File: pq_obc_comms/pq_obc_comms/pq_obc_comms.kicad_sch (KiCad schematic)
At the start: 66 parts, among them J1 Conn_01x10, J2 Conn_01x10, J3 Conn_01x10, J4 Conn_01x10, J6 U.FL-R-SMT-1_10_, U1 STM32L476RGTx, U2 SX1262IMLTRT, U3 BD2232G-GTR, U4 BD2232G-GTR, U5 RFswitch, U7 BD2232G-GTR, X1 12MHz, X2 FA-128_32.0000MF20X-K5, X3 32.768KHz

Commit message: Cleanup!
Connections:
- net 3V3: no longer J1.10 (Pin_10)
- new net 3V3_PERM: J1.10 (Pin_10)
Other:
- moved on the sheet: C45, J3, U3

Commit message: obc rework
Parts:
- removed C40, C41: 20pF, symbol COMMS-altium-import:3_20pF
- removed D2: VCC_TEST, symbol COMMS-altium-import:0_VCC_TEST
- removed J6: U.FL-R-SMT-1_10_, symbol COMMS-altium-import:1_U.FL-R-SMT-1_10_
- removed PROBE1: MS-156C, GGS_Connectors:CoaxialSwitch_Hirose_MS-156C3_Horizontal, symbol GGS_Connectors:MS-156C
- removed X1: 12MHz, GGS_Miscellaneous:ECX-32, symbol COMMS-altium-import:0_12MHz
- added C40: 20pF, Capacitor_SMD:C_0603_1608Metric, symbol COMMS-altium-import:3_10pF
- added C41: 20pF, Capacitor_SMD:C_0603_1608Metric, symbol COMMS-altium-import:3_100nF
- added D2: RBS1LAM40ATR, Diode_SMD:D_SOD-128, symbol Simulation_SPICE:DIODE
- added J6: U.FL-R-SMT-1_10, Connector_Coaxial:U.FL_Hirose_U.FL-R-SMT-1_Vertical, symbol Connector:Conn_Coaxial
- added TP1: CoaxialSwitch_Testpoint, symbol Connector:CoaxialSwitch_Testpoint
- added X1: ECS-120-18-33-JEM-TR3, GGS_Miscellaneous:ECX-32, symbol Device:Crystal_GND24
- C1, C11, C12, C2, C4, C5, C6, C7, C8: footprint (none) -> Capacitor_SMD:C_0402_1005Metric
- C10, C9: footprint (none) -> Capacitor_SMD:C_0402_1005Metric; symbol COMMS-altium-import:3_3.3pF -> Device:C
- C14, C15, C16, C17, C18, C27, C28, C42, C43, C44, C45: footprint (none) -> Capacitor_SMD:C_0603_1608Metric
- D1: value VCC -> RBS1LAM40ATR; footprint (none) -> Diode_SMD:D_SOD-128; BOM_JLCPCB PART CLASS Extended Part -> (none); BOM_MANUFACTURER ROHM Semicon -> (none); BOM_MANUFACTURER PART PDZVTR4.7B -> (none); BOM_SUPPLIER LCSC -> (none); BOM_SUPPLIER PART C253498 -> (none)
- L1, L2, L3, L4, L5, L6: footprint (none) -> Inductor_SMD:L_0402_1005Metric
- L7: footprint (none) -> Inductor_SMD:L_0805_2012Metric
- R3, R4, R6, R7, R8: footprint (none) -> Resistor_SMD:R_0603_1608Metric
- U2: footprint (none) -> Package_DFN_QFN:QFN-24-1EP_4x4mm_P0.5mm_EP2.6x2.6mm
- U3, U4, U7: footprint (none) -> Package_TO_SOT_SMD:SOT-23-5
- U5: value RFswitch -> BGS12PL6E6327XTSA1; footprint (none) -> GGS_RF:PG-TSLP-6-4; BOM_SUPPLIER PART C1854968 -> BGS12PL6E6327XTSA1
- X3: value 32.768KHz -> ABS09-32.768KHZ-7-T; footprint (none) -> GGS_Miscellaneous:ABS09; BOM_SUPPLIER LCSC -> (none); BOM_SUPPLIER PART C1985392 -> (none)
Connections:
- net ADC_PH: now also J4.5 (Pin_5); no longer J4.6 (Pin_6)
- net ADC_PL: now also J2.9 (Pin_9); no longer J2.2 (Pin_2)
- net CHRG: now also J4.10 (Pin_10); no longer J4.1 (Pin_1)
- net CHRGOFF: now also J2.4 (Pin_4); no longer J2.7 (Pin_7)
- net CLPROG: now also J2.3 (Pin_3); no longer J2.8 (Pin_8)
- net DAC_PL: now also J2.8 (Pin_8); no longer J2.3 (Pin_3)
- net EPS_RST: no longer J3.10 (Pin_10)
- net FAULT: now also J4.9 (Pin_9); no longer J4.2 (Pin_2)
- net GND: now also C40.2, C41.2, J6.2 (Ext), TP1.G, X1.2, X1.4
- net MPPT_X: no longer J2.9 (Pin_9)
- net MPPT_Y: no longer J4.8 (Pin_8)
- net MPPT_Z: no longer J4.9 (Pin_9)
- net NRST: now also J2.5 (Pin_5); no longer J2.6 (Pin_6)
- net OSC_IN: now also C40.1, X1.1
- net OSC_OUT: now also C41.1, X1.3
- net P/L_POWER: now also J4.6 (Pin_6); no longer J4.5 (Pin_5)
- net RST_DRIVERS: now also J4.4 (Pin_4); no longer J4.7 (Pin_7)
- net SEL_PH0: now also J4.7 (Pin_7); no longer J4.4 (Pin_4)
- net SOLAR_X: now also J2.1 (Pin_1); no longer J2.10 (Pin_10)
- net SOLAR_Z: now also J4.1 (Pin_1); no longer J4.10 (Pin_10)
- net STM32_PA2: now also J2.10 (Pin_10); no longer J2.1 (Pin_1)
- net STM32_PD2: now also J4.2 (Pin_2); no longer J3.3 (Pin_3)
- net SWCLK: now also J2.7 (Pin_7); no longer J2.4 (Pin_4)
- net SWDIO: now also J2.6 (Pin_6); no longer J2.5 (Pin_5)
- net VCC: now also D2.2 (K); no longer J4.3 (Pin_3)
- net at L2.2: now also TP1.C
- net at C10.1, L5.2: now also J6.1 (In)
- net at C4.1, L1.2, L3.1: now also TP1.A
- net P/L2BURN renamed ADCS_POWER
- net ADCS_POWER: now also J4.3 (Pin_3)
- new net BATT_NTC: J3.3 (Pin_3)
- new net VCC_UMBILICAL: D2.1 (A), J4.8 (Pin_8)
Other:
- note removed: "To be done in PL2 board"
- note removed: "Vcc Test"
- moved on the sheet: C1, C14, C2, C27, C28, C31, C32, C33, C34, C35, C36, C37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

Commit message: OBC board revision 3 finished
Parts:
- added C3: 100nF, Capacitor_SMD:C_0603_1608Metric, symbol Device:C
- TP1: footprint (none) -> Connector_Coaxial:CoaxialSwitch_Hirose_MS-156C3_Horizontal
- X2: footprint (none) -> GGS_Miscellaneous:EPSON_FA128
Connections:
- net 3V3 is gone; now on net 3V3_PERM: D1.1 (A)
- net BUSY is gone; now on net SX1262_BUSY: U1.41 (PA8)
- net CHGOFF is gone; now on net CHRGOFF: U1.8 (PC0)
- net P/L2BURN_OBC is gone; now on net PoL_ADCS_POWER_EN: U4.3 (EN/EN#)
- net SEL_PH3 is gone; now on net SEL_PH0: U1.10 (PC2)
- net GND: now also J3.10 (Pin_10), C3.2
- net PoL_P/L_EN: now also U1.37 (PC6); no longer U1.11 (PC3)
- net VCC: now also C3.1
- net RFswitch_Vcc: now reaches C14.1, R4.2, U5.4 (VDD)
- net DIO2: now reaches R3.1, U2.12 (DIO2)
- net EPS_RST renamed STM32_PB0
- net STM32_PB0: now also J4.2 (Pin_2)
- net MPPT_X: no longer names the net of U1.22 (PA6)
- net MPPT_Y: no longer names the net of U1.27 (PB1)
- net MPPT_Z renamed PoL_ADCS_POWER_EN
- net STM32_PD2: no longer names the net of U1.54 (PD2)
- net STM32_PD2: no longer J4.2 (Pin_2)
- no-connect marks 14 -> 13
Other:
- moved on the sheet: C14, C16, C18, R4

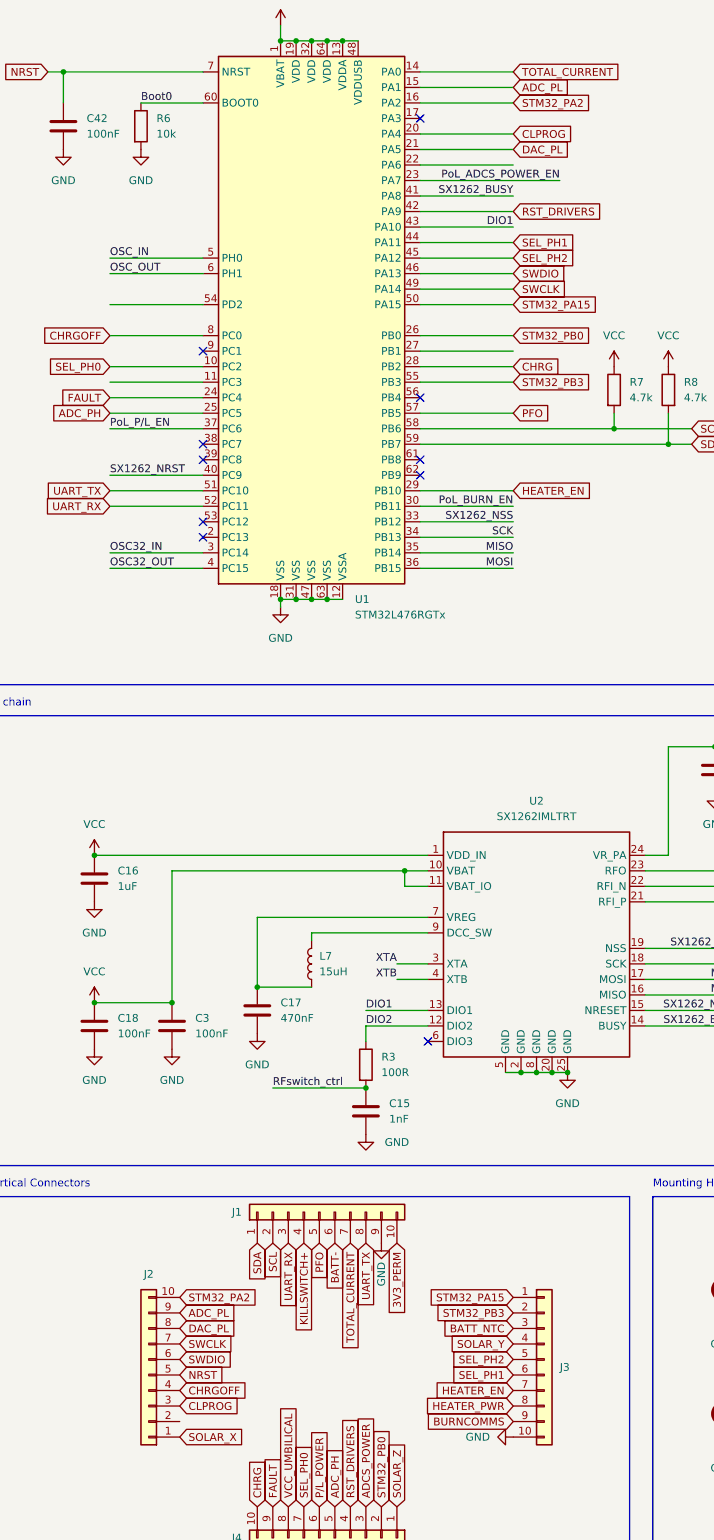
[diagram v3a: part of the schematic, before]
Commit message: added PA3 pin to pinout
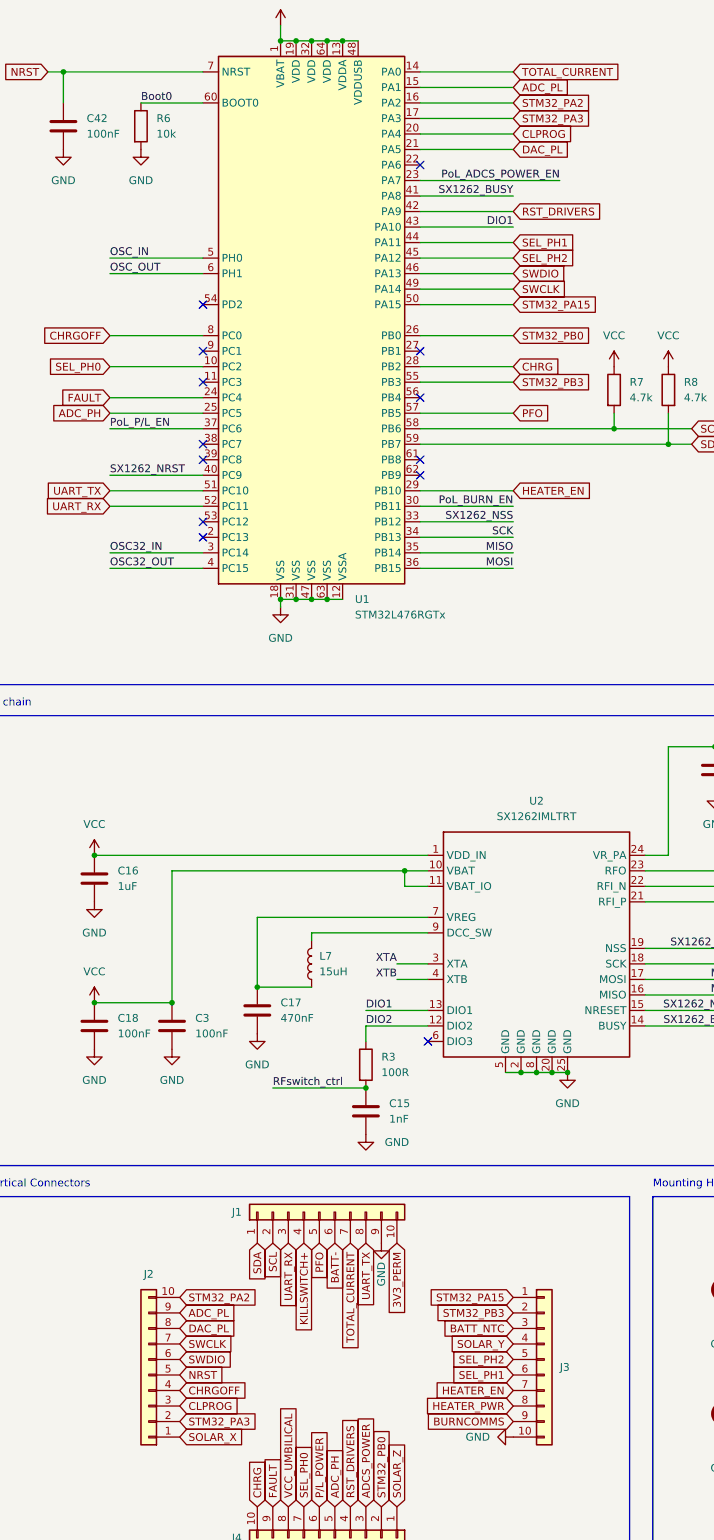
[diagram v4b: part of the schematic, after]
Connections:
- net STM32_PA3: now reaches U1.17 (PA3)
- net STM32_PA3: now also J2.2 (Pin_2)
- no-connect marks 13 -> 16
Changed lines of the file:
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@@
   (no_connect (at 92.71 91.44))
   (no_connect (at 378.46 207.01))
+  (no_connect (at 57.15 76.2))
+  (no_connect (at 57.15 88.9))
+  (no_connect (at 92.71 83.82))
+  (no_connect (at 92.71 53.34))
   (no_connect (at 57.15 111.76))
   (no_connect (at 57.15 99.06))
   (no_connect (at 57.15 101.6))
   (no_connect (at 378.46 165.1))
-  (no_connect (at 92.71 45.72))
   (no_connect (at 92.71 104.14))
   (no_connect (at 92.71 101.6))
@@
     (stroke (width 0) (type default) (color 0 0 0 0))
   )
-  (wire (pts (xy 107.95 53.34) (xy 92.71 53.34))
-    (stroke (width 0) (type default) (color 0 0 0 0))
-  )
   (wire (pts (xy 331.47 162.56) (xy 340.36 162.56))
     (stroke (width 0.254) (type default) (color 0 0 0 0))
@@
     (stroke (width 0.254) (type default) (color 0 0 0 0))
   )
+  (wire (pts (xy 107.95 45.72) (xy 92.71 45.72))
+    (stroke (width 0) (type default) (color 0 0 0 0))
+  )
   (wire (pts (xy 107.95 40.64) (xy 92.71 40.64))
     (stroke (width 0) (type default) (color 0 0 0 0))
@@
     (stroke (width 0.254) (type default) (color 0 0 0 0))
   )
-  (wire (pts (xy 41.91 76.2) (xy 57.15 76.2))
-    (stroke (width 0) (type default) (color 0 0 0 0))
-  )
   (wire (pts (xy 184.15 110.49) (xy 184.15 106.68))
     (stroke (width 0.254) (type default) (color 0 0 0 0))
@@
     (stroke (width 0) (type default) (color 0 0 0 0))
   )
-  (wire (pts (xy 107.95 83.82) (xy 92.71 83.82))
-    (stroke (width 0) (type default) (color 0 0 0 0))
-  )
   (wire (pts (xy 224.79 45.9741) (xy 224.79 42.1641))
     (stroke (width 0.254) (type default) (color 0 0 0 0))
@@
   )
   (wire (pts (xy 147.32 173.99) (xy 129.54 173.99))
-    (stroke (width 0) (type default) (color 0 0 0 0))
-  )
-  (wire (pts (xy 41.91 88.9) (xy 57.15 88.9))
     (stroke (width 0) (type default) (color 0 0 0 0))
   )
@@
     )
   )
+  (global_label "STM32_PA3" (shape input) (at 107.95 45.72 0) (fields_autoplaced)
+    (effects (font (size 1.27 1.27)) (justify left))
+    (property "Intersheet References" "${INTERSHEET_REFS}" (id 0) (at 120.9464 45.6406 0)
+      (effects (font (size 1.27 1.27)) (justify left) hide)
+    )
+  )
   (global_label "SCL" (shape input) (at 68.58 229.87 270) (fields_autoplaced)
     (effects (font (size 1.27 1.27)) (justify right))
@@
       (effects (font (size 1.27 1.27)) (justify left) hide)
     )
+  )
+  (global_label "STM32_PA3" (shape input) (at 53.34 259.08 0) (fields_autoplaced)
+    (effects (font (size 1.27 1.27)) (justify left))
+    (property "Intersheet References" "${INTERSHEET_REFS}" (id 0) (at 66.3364 259.0006 0)
+      (effects (font (size 1.27 1.27)) (justify left) hide)
+    )
